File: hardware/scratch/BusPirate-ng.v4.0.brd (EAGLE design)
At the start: 100 x 50 mm, 136 parts, among them IC1 IC_MEM_23LC1024, IC10 IC_BUFF_SN74LVC1T45DBV, IC11 IC_BUFF_SN74LVC1T45DBV, IC12 74LVC1G07DBV, IC13 IC_BUFF_SN74LVC1T45DBV, IC14 IC_BL1551, IC15 IC_BL1551, IC16 74HCT4066PW, IC2 IC_MEM_23LC1024, IC3 IC_74AC573, IC4 74LVC1G07DBV, IC5 74LVC1G07DBV, IC6 74LVC1G07DBV, IC7 74LVC1G07DBV, IC8 IC_BUFF_SN74LVC1T45DBV, IC9 IC_BUFF_SN74LVC1T45DBV, J1 CON_HEADER_2X02-PTH, J2 CON_HEADER_1X04, J3 CON_HEADER_1X03-PTH, J4 CON_HEADER_1X10-RIGHT_ANGLED_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, U1 IC_MEM_AT45DB041D, U2 IC_UC_STM32F103ZX, U3 IC_FPGA_ICE40HX4K

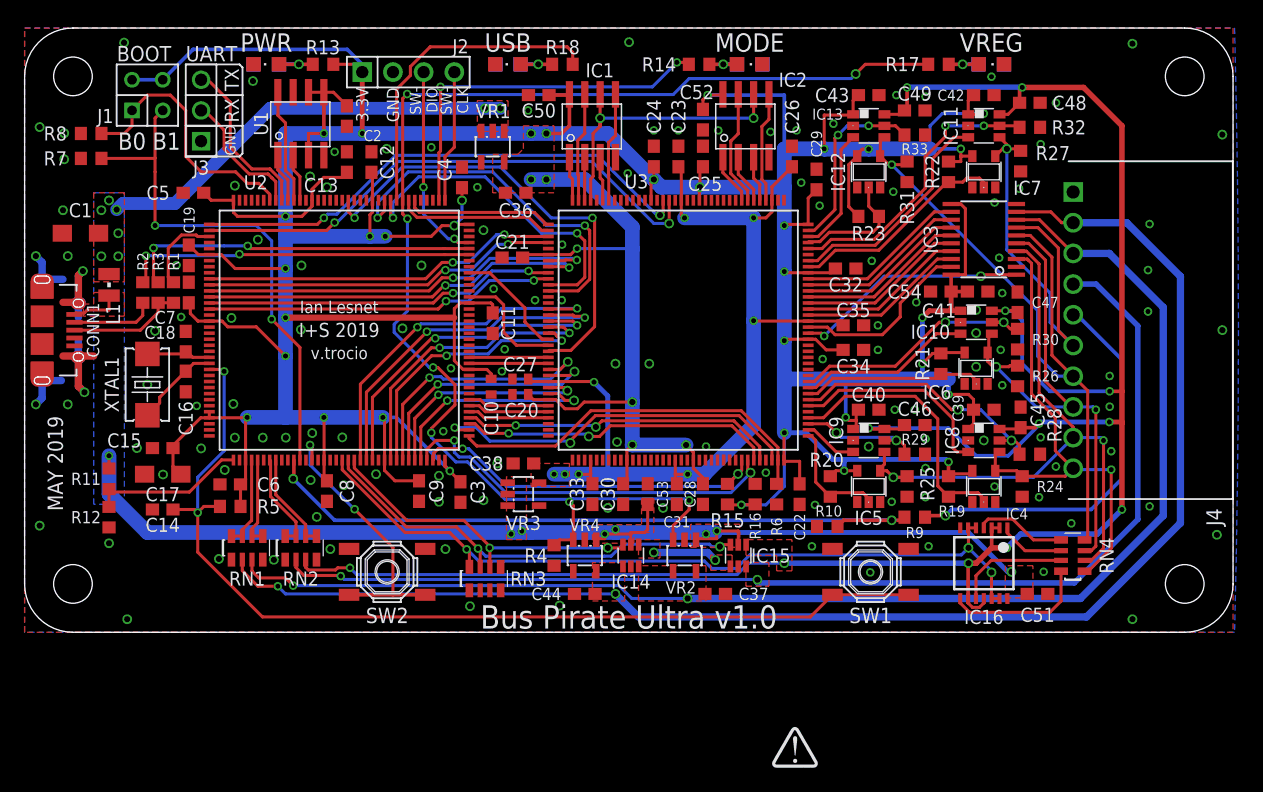
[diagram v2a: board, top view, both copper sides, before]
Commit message: Auxillary connection from MCU to FPGA -MCU_AUX1 FPGA_137 -> PC10 -MCU_AUX2 FPGA_136 -> PC11 -MCU_AUX3 FPGA_135 -> PC12 -MCU_AUX4 FPGA_134 -> PD6 -MCU_AUX5 FPGA_125 -> PB8 -MCU_AUX6 FPGA_124 -> PB9 -MCU_AUX7 FPGA_119 -> PE0 -MCU_AUX8 FPGA_118 -> PE1
gave SRAM each FPGA clock pins, SRAM0_CLOCK and SRAM1_CLOCK
-moved around SRAM1's pins of FPGA
-SRAM1_CS from FPGA_116 to FPGA_117
-SRAM1_SIO3 from FPGA_115 to FPGA_116
-SRAM_SIO1 from FPGA_114 to FPGA_115
-new FPGA pin SRAM1_CLOCK to FPGA_114
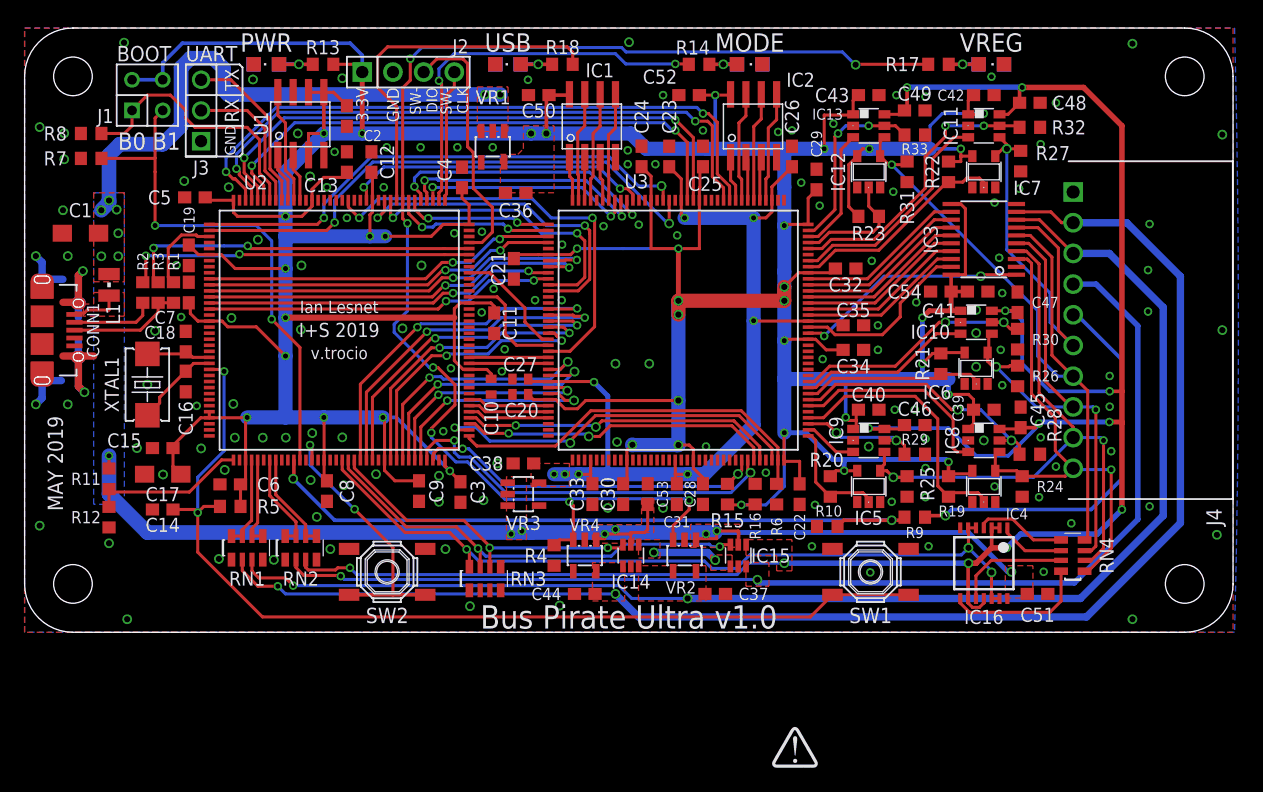
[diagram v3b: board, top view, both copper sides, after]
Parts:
- moved C52 2.33 mm to (55.0, 44.5), turned to 180 degrees
- moved C24 1.02 mm to (51.1, 39.4)
- moved C21 0.95 mm to (40.5, 30.1), turned to 90 degrees
- moved C23 0.76 mm to (53.3, 39.4)
- moved IC2 0.64 mm to (60.3, 41.9)
- moved C5 0.40 mm to (14.1, 36.0)
- moved C11 0.13 mm to (38.9, 25.6)
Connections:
- removed net N$11: U3.125
- removed net N$12: U3.124
- removed net N$26: U3.119
- removed net N$32: U2.139
- removed net N$33: U2.140
- removed net N$48: U3.117
- removed net N$49: U3.118
- removed net SRAM_CLOCK: IC1.6, IC2.6, U3.141
- new net MCU_AUX1: U2.111, U3.137
- new net MCU_AUX2: U2.112, U3.136
- new net MCU_AUX3: U2.113, U3.135
- new net MCU_AUX4: U2.122, U3.134
- new net MCU_AUX5: U2.139, U3.125
- new net MCU_AUX6: U2.140, U3.124
- new net MCU_AUX7: U2.141, U3.119
- new net MCU_AUX8: U2.142, U3.118
- new net N$21: U3.130
- new net N$56: U2.123
- new net N$57: U2.126
- new net N$58: U2.127
- new net N$59: U2.128
- new net N$60: U2.129
- new net N$61: U2.132
- new net SRAM0_CLOCK: IC1.6, U3.141
- new net SRAM1_CLOCK: IC2.6, U3.114
- net SRAM1_CS: now also U3.117; no longer U3.116
- net SRAM1_SIO1: now also U3.115; no longer U3.114
- net SRAM1_SIO3: now also U3.116; no longer U3.115
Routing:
- net MCU_AUX8: track 0.00 -> 54.1 mm, vias 0 -> 2
- net MCU_AUX7: track 0.00 -> 52.2 mm, vias 0 -> 2
- net MCU_AUX6: track 0.00 -> 48.4 mm, vias 0 -> 2
- net MCU_AUX5: track 0.00 -> 46.2 mm, vias 0 -> 2
- net MCU_AUX4: track 0.00 -> 25.6 mm, vias 0 -> 2
- net SRAM_CLOCK: track 24.4 -> 0.00 mm, vias 2 -> 0
- net MCU_AUX3: track 0.00 -> 23.2 mm, vias 0 -> 2
- net MCU_AUX2: track 0.00 -> 20.8 mm, vias 0 -> 2
- net MCU_AUX1: track 0.00 -> 18.3 mm, vias 0 -> 2
- net 3V3: track 495.8 -> 506.6 mm, vias 40 -> 38
- net VUSB: track 140.9 -> 151.3 mm
- net SRAM0_CLOCK: track 0.00 -> 9.16 mm
- net SRAM1_CLOCK: track 0.00 -> 9.02 mm
- net SWDIO: track 16.5 -> 21.3 mm, vias 2 -> 0
- net USBLED: track 26.8 -> 30.2 mm
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
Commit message: added new aux pins connecting MCU to FPGA, created gerbers for BP ultra and BP ultra testboard
Moved pins to make way for AUX pins connection
-swapped MCU pins PB10(FPGA_CRESET) and PB11(FPGA_CDONE)
-moved VREGEN from MCU pin PD2 to PF14

New aux pins connecting MCU to FPGA
-MCU_AUX9 FPGA_37 PF13
-MCU_AUX10 FPGA_38 PB0
-MCU_AUX11 FPGA_39 PC5
-MCU_AUX12 FPGA_41 PA6
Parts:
- moved C29 0.51 mm to (66.0, 37.5)
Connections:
- removed net N$15: U2.54
- removed net N$25: U2.45
- removed net N$42: U2.42
- removed net N$44: U2.46
- new net MCU_AUX10: U2.46, U3.38
- new net MCU_AUX11: U2.45, U3.39
- new net MCU_AUX12: U2.42, U3.41
- new net MCU_AUX9: U2.53, U3.37
- net FPGA_CDONE: now also U2.69; no longer U2.70
- net FPGA_CRESET: now also U2.70; no longer U2.69
- net VREGEN: now also U2.54; no longer U2.116
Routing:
- net MCU_AUX12: track 0.00 -> 38.8 mm, vias 0 -> 2
- net MCU_AUX11: track 0.00 -> 35.9 mm, vias 0 -> 2
- net MCU_AUX10: track 0.00 -> 33.7 mm, vias 0 -> 2
- net MCU_AUX9: track 0.00 -> 28.5 mm, vias 0 -> 2
- net VREGEN: track 112.0 -> 91.9 mm, vias 7 -> 4
- net 3V3: track 506.6 -> 511.6 mm
- net FPGA_PROG_CS: track 31.6 -> 35.7 mm, vias 0 -> 2
- net 1V2: track 80.5 -> 84.3 mm
- net FPGA_CRESET: track 33.3 -> 31.5 mm
- net FSMC_D12: track 18.7 -> 20.3 mm
- net FPGA_CDONE: track 30.1 -> 31.1 mm
- net GND: vias 146 -> 150

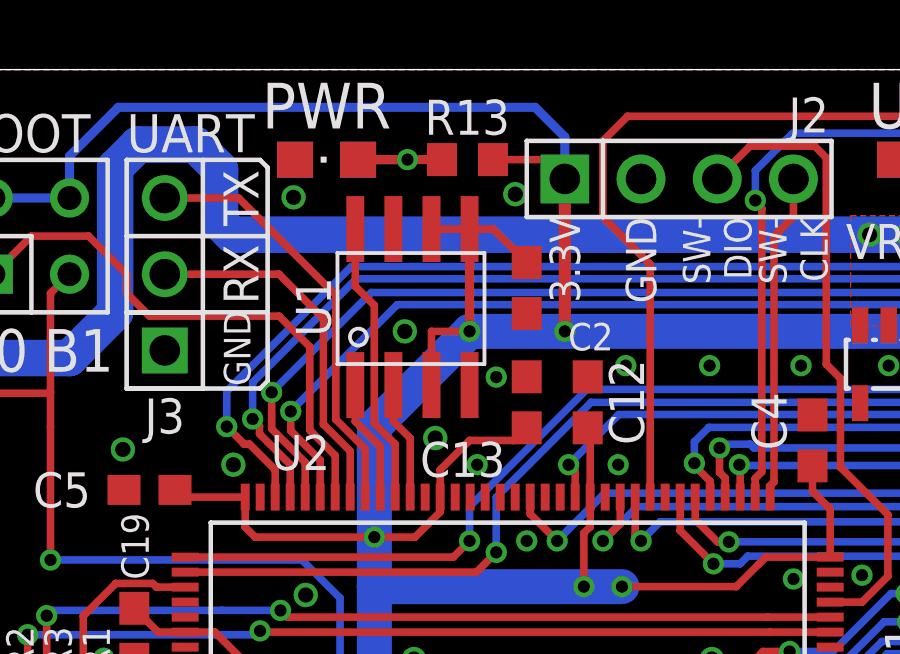
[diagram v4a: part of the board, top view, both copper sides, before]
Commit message: replaced U1 flash chip of BP ultra to W25X40CL type, still an SO-8 footprint
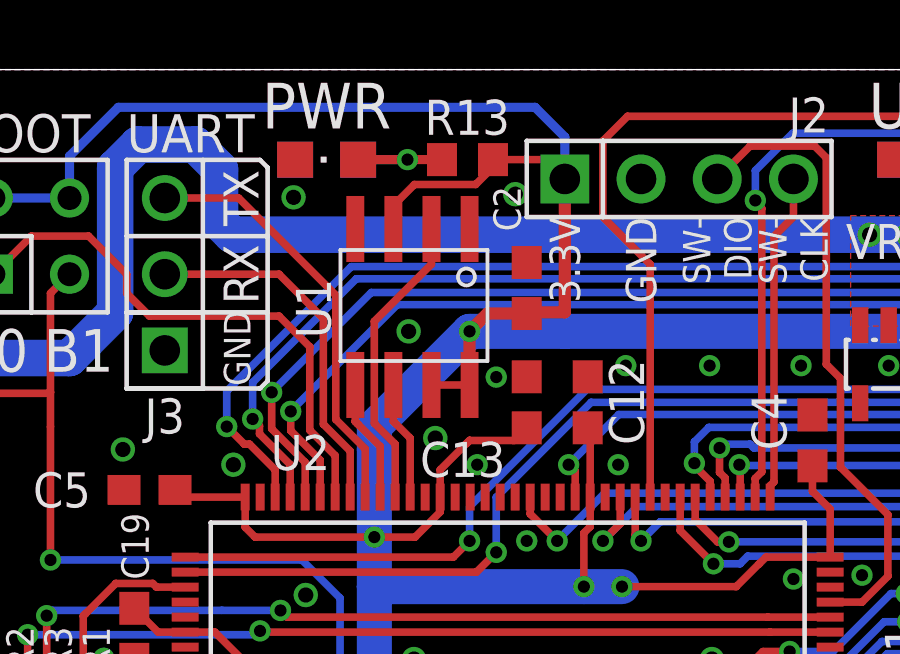
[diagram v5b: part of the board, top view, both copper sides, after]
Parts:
- U1: value IC_MEM_AT45DB041D -> IC_MEM_W25X40CL
- turned U1 to 180 degrees
- turned C2 to 270 degrees
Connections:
- net 3V3: now also U1.7, U1.8; no longer U1.5, U1.6
- net FLASH_MISO: now also U1.2; no longer U1.8
- net FLASH_MOSI: now also U1.5; no longer U1.1
- net FLASH_SCK: now also U1.6; no longer U1.2
- net GND: now also U1.1; no longer U1.7
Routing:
- net 3V3: track 511.6 -> 512.4 mm, vias 38 -> 37
- net FLASH_MISO: track 9.49 -> 10.0 mm
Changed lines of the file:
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@@
 <attribute name="VALUE" x="11.43" y="24.686" size="1.27" layer="27" rot="R270"/>
-</element>
-<element name="U1" library="dp_devices.v6" package="SOIC-8" value="IC_MEM_AT45DB041D" x="22.86" y="42.085" smashed="yes">
-<attribute name="NAME" x="19.558" y="42.0878" size="1.1684" layer="25" font="vector" ratio="12" rot="R270" align="center"/>
-<attribute name="VALUE" x="27.305" y="40.18" size="1.27" layer="27" font="vector" ratio="10" rot="R90"/>
 </element>
 <element name="C35" library="rcl" package="C0603" value="0.1uF" x="68.58" y="25.4" smashed="yes" rot="R180">
@@
 <attribute name="VALUE" x="64.135" y="38.1" size="1.27" layer="27" rot="R270"/>
 </element>
-<element name="C2" library="rcl" package="C0603" value="0.1uF" x="26.67" y="42.72" smashed="yes" rot="R90">
-<attribute name="NAME" x="28.8036" y="41.0972" size="0.9144" layer="25" font="vector" ratio="15" align="center"/>
-<attribute name="VALUE" x="28.575" y="42.085" size="1.27" layer="27" rot="R90"/>
+<element name="C2" library="rcl" package="C0603" value="0.1uF" x="26.67" y="42.72" smashed="yes" rot="R270">
+<attribute name="NAME" x="26.0152" y="45.3644" size="0.9144" layer="25" font="vector" ratio="15" rot="R270" align="center"/>
+<attribute name="VALUE" x="24.765" y="43.355" size="1.27" layer="27" rot="R270"/>
 </element>
 <element name="C22" library="rcl" package="C0603" value="0.1uF" x="64.135" y="11.43" smashed="yes" rot="R90">
@@
 </element>
 <element name="CONN1" library="dp_devices.v6" package="CON_USB_MICRO-B-2-SD-47589-001" value="CON-USB-F-MICRO-B-2" x="1.1" y="25" rot="R270"/>
+<element name="U1" library="dp_devices.v6" package="SOIC-8" value="IC_MEM_W25X40CL" x="22.86" y="42.0878" smashed="yes" rot="R180">
+<attribute name="NAME" x="19.558" y="42.037" size="1.1684" layer="25" font="vector" ratio="12" rot="R270" align="center"/>
+<attribute name="VALUE" x="18.415" y="43.9928" size="1.27" layer="27" font="vector" ratio="10" rot="R270"/>
+</element>
 </elements>
 <signals>
@@
 <contactref element="C16" pad="1"/>
 <contactref element="C18" pad="1"/>
-<contactref element="U1" pad="7"/>
 <contactref element="C35" pad="1"/>
 <contactref element="C34" pad="1"/>
@@
 <contactref element="U2" pad="107"/>
 <contactref element="U2" pad="71"/>
-<contactref element="C2" pad="1"/>
-<contactref element="U1" pad="4"/>
 <contactref element="C22" pad="1"/>
 <contactref element="C21" pad="1"/>
@@
 <via x="54.0004" y="32.8422" extent="1-16" drill="0.4064"/>
 <via x="26.67" y="34.29" extent="1-16" drill="0.4064"/>
-<via x="22.606" y="41.275" extent="1-16" drill="0.508"/>
+<via x="22.733" y="41.275" extent="1-16" drill="0.508"/>
 <via x="26.289" y="45.847" extent="1-16" drill="0.508"/>
 <via x="13.208" y="37.338" extent="1-16" drill="0.508"/>
@@
 <via x="58.547" y="15.748" extent="1-16" drill="0.4064"/>
 <via x="19.812" y="19.4564" extent="1-16" drill="0.508"/>
+<contactref element="U1" pad="4"/>
+<contactref element="U1" pad="1"/>
+<contactref element="C2" pad="1"/>
 </signal>
 <signal name="3V3">
@@
 <contactref element="U3" pad="131"/>
 <contactref element="C24" pad="2"/>
-<contactref element="U1" pad="6"/>
-<contactref element="C2" pad="2"/>
 <contactref element="U3" pad="72"/>
 <contactref element="C22" pad="2"/>
@@
 <wire x1="38.248859375" y1="21.75" x2="36.785" y2="21.75" width="0.254" layer="1"/>
 <wire x1="23.785" y1="35.75" x2="23.785" y2="36.66" width="0.254" layer="1"/>
-<wire x1="23.785" y1="36.66" x2="24.765" y2="37.64" width="0.254" layer="1"/>
+<wire x1="23.785" y1="36.66" x2="24.6775" y2="37.5525" width="0.254" layer="1"/>
+<wire x1="24.6775" y1="37.5525" x2="24.765" y2="37.64" width="0.254" layer="1"/>
 <wire x1="24.765" y1="37.64" x2="26.25" y2="37.64" width="0.254" layer="1"/>
 <wire x1="26.25" y1="37.64" x2="26.67" y2="38.06" width="0.254" layer="1"/>
-<contactref element="U1" pad="3"/>
-<contactref element="U1" pad="5"/>
 <wire x1="62.8393" y1="14.25" x2="62.9443" y2="14.145" width="0.254" layer="1"/>
 <wire x1="62.9443" y1="14.145" x2="64.135" y2="14.145" width="0.254" layer="1"/>
@@
 <wire x1="27.94" y1="47.752" x2="27.94" y2="46.355" width="0.3048" layer="16"/>
 <wire x1="13.055975" y1="48.742975" x2="26.949025" y2="48.742975" width="0.3048" layer="16"/>
-<wire x1="23.495" y1="44.685" x2="24.765" y2="44.685" width="0.254" layer="1"/>
-<wire x1="24.765" y1="44.685" x2="25.555" y2="44.685" width="0.254" layer="1"/>
-<wire x1="25.555" y1="44.685" x2="26.67" y2="43.57" width="0.254" layer="1"/>
 <wire x1="15.285" y1="17.75" x2="14.575" y2="17.75" width="0.254" layer="1"/>
 <wire x1="12.28" y1="15.455" x2="12.28" y2="15.24" width="0.254" layer="1"/>
@@
 <wire x1="22.94713125" y1="34.417" x2="21.59" y2="34.417" width="0.254" layer="1"/>
 <wire x1="23.785" y1="35.75" x2="23.785" y2="35.25486875" width="0.254" layer="1"/>
-<wire x1="24.765" y1="44.685" x2="24.765" y2="41.275" width="0.3048" layer="1"/>
 <via x="24.765" y="41.275" extent="1-16" drill="0.4064"/>
-<wire x1="23.495" y1="39.485" x2="23.495" y2="41.275" width="0.254" layer="1"/>
-<wire x1="23.495" y1="41.275" x2="24.765" y2="41.275" width="0.254" layer="1"/>
-<wire x1="27.94" y1="46.355" x2="27.94" y2="41.275" width="0.4064" layer="1"/>
-<via x="27.94" y="41.275" extent="1-16" drill="0.4064"/>
+<wire x1="27.94" y1="46.355" x2="27.94" y2="41.91" width="0.4064" layer="1"/>
 <wire x1="17.285" y1="34.74686875" x2="17.61486875" y2="34.417" width="0.254" layer="1"/>
 <wire x1="17.61486875" y1="34.417" x2="21.59" y2="34.417" width="0.254" layer="1"/>
@@
 <wire x1="18.415" y1="21.59" x2="19.685" y2="22.86" width="1.1684" layer="16"/>
 <wire x1="19.685" y1="22.86" x2="21.59" y2="22.86" width="1.1684" layer="16"/>
+<contactref element="U1" pad="7"/>
+<contactref element="U1" pad="3"/>
+<contactref element="U1" pad="8"/>
+<contactref element="C2" pad="2"/>
+<wire x1="24.6775" y1="37.5525" x2="24.765" y2="37.64" width="0.254" layer="1"/>
+<wire x1="23.495" y1="39.4878" x2="24.765" y2="39.4878" width="0.254" layer="1"/>
+<wire x1="22.225" y1="45.46693125" x2="22.92866875" y2="46.1706" width="0.254" layer="1"/>
+<wire x1="24.96873125" y1="46.1706" x2="25.545" y2="46.74686875" width="0.254" layer="1"/>
+<wire x1="22.92866875" y1="46.1706" x2="24.96873125" y2="46.1706" width="0.254" layer="1"/>
+<wire x1="25.545" y1="46.74686875" x2="25.545" y2="47" width="0.254" layer="1"/>
+<wire x1="22.225" y1="44.6878" x2="22.225" y2="45.46693125" width="0.254" layer="1"/>
+<wire x1="24.765" y1="39.4878" x2="24.765" y2="41.275" width="0.4064" layer="1"/>
+<wire x1="26.67" y1="41.87" x2="25.36" y2="41.87" width="0.4064" layer="1"/>
+<wire x1="25.36" y1="41.87" x2="24.765" y2="41.275" width="0.4064" layer="1"/>
+<wire x1="26.67" y1="41.87" x2="26.71" y2="41.91" width="0.4064" layer="1"/>
+<wire x1="26.71" y1="41.91" x2="27.94" y2="41.91" width="0.4064" layer="1"/>
 </signal>
 <signal name="N$7">
@@
 </signal>
 <signal name="FLASH_SCK">
-<contactref element="U1" pad="2"/>
 <contactref element="U2" pad="133"/>
 <wire x1="22.785" y1="35.75" x2="22.785" y2="37.715" width="0.254" layer="1"/>
-<wire x1="22.785" y1="37.715" x2="22.225" y2="38.275" width="0.254" layer="1"/>
-<wire x1="22.225" y1="38.275" x2="22.225" y2="39.485" width="0.254" layer="1"/>
+<wire x1="22.785" y1="37.715" x2="22.3125" y2="38.1875" width="0.254" layer="1"/>
+<contactref element="U1" pad="6"/>
+<wire x1="22.3125" y1="38.1875" x2="22.225" y2="38.275" width="0.254" layer="1"/>
+<wire x1="22.3125" y1="38.1875" x2="22.225" y2="38.275" width="0.254" layer="1"/>
+<wire x1="22.225" y1="38.275" x2="22.225" y2="39.4878" width="0.254" layer="1"/>
 </signal>
 <signal name="FLASH_MISO">
-<contactref element="U1" pad="8"/>
 <contactref element="U2" pad="134"/>
 <wire x1="22.285" y1="37.51513125" x2="21.59" y2="38.21013125" width="0.254" layer="1"/>
-<wire x1="21.59" y1="38.21013125" x2="21.59" y2="42.145" width="0.254" layer="1"/>
-<wire x1="20.955" y1="42.78" x2="20.955" y2="44.685" width="0.254" layer="1"/>
-<wire x1="21.59" y1="42.145" x2="20.955" y2="42.78" width="0.254" layer="1"/>
+<wire x1="21.59" y1="38.21013125" x2="21.59" y2="41.60986875" width="0.254" layer="1"/>
 <wire x1="22.285" y1="35.75" x2="22.285" y2="37.51513125" width="0.254" layer="1"/>
+<contactref element="U1" pad="2"/>
+<wire x1="23.495" y1="43.51486875" x2="23.495" y2="44.6878" width="0.254" layer="1"/>
+<wire x1="21.59" y1="41.60986875" x2="23.495" y2="43.51486875" width="0.254" layer="1"/>
 </signal>
 <signal name="FLASH_MOSI">
-<contactref element="U1" pad="1"/>
 <contactref element="U2" pad="135"/>
 <wire x1="21.785" y1="35.75" x2="21.785" y2="37.44039375" width="0.254" layer="1"/>
-<wire x1="21.785" y1="37.44039375" x2="20.955" y2="38.27039375" width="0.254" layer="1"/>
-<wire x1="20.955" y1="38.27039375" x2="20.955" y2="39.485" width="0.254" layer="1"/>
+<wire x1="21.785" y1="37.44039375" x2="21.040196875" y2="38.185196875" width="0.254" layer="1"/>
+<contactref element="U1" pad="5"/>
+<wire x1="21.040196875" y1="38.185196875" x2="20.955" y2="38.27039375" width="0.254" layer="1"/>
+<wire x1="21.040196875" y1="38.185196875" x2="20.955" y2="38.27039375" width="0.254" layer="1"/>
+<wire x1="20.955" y1="38.27039375" x2="20.955" y2="39.4878" width="0.254" layer="1"/>
 </signal>
 <signal name="FSMC_D8">
